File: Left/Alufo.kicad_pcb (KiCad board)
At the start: 2 copper layers, 139.7 x 88.9 mm, 67 parts, among them J1 USB_C_Receptacle_USB2.0_16P_2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, J3 USB_C_Receptacle_USB2.0_16P_2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, K11 PG1350, K12 PG1350, K13 PG1350, K14 PG1350, K15 PG1350, K16 PG1350, K21 PG1350, K22 PG1350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

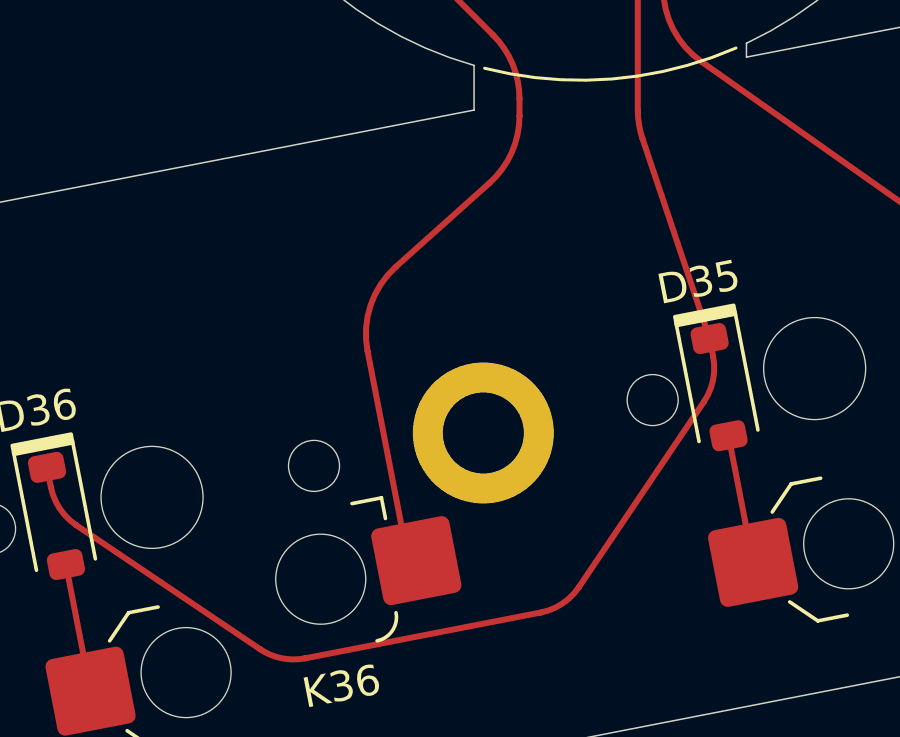
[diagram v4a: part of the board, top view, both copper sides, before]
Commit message: Fix alignment of thumb cluster screw hole
It did not line up when one side’s PCB was used as a base for the other.
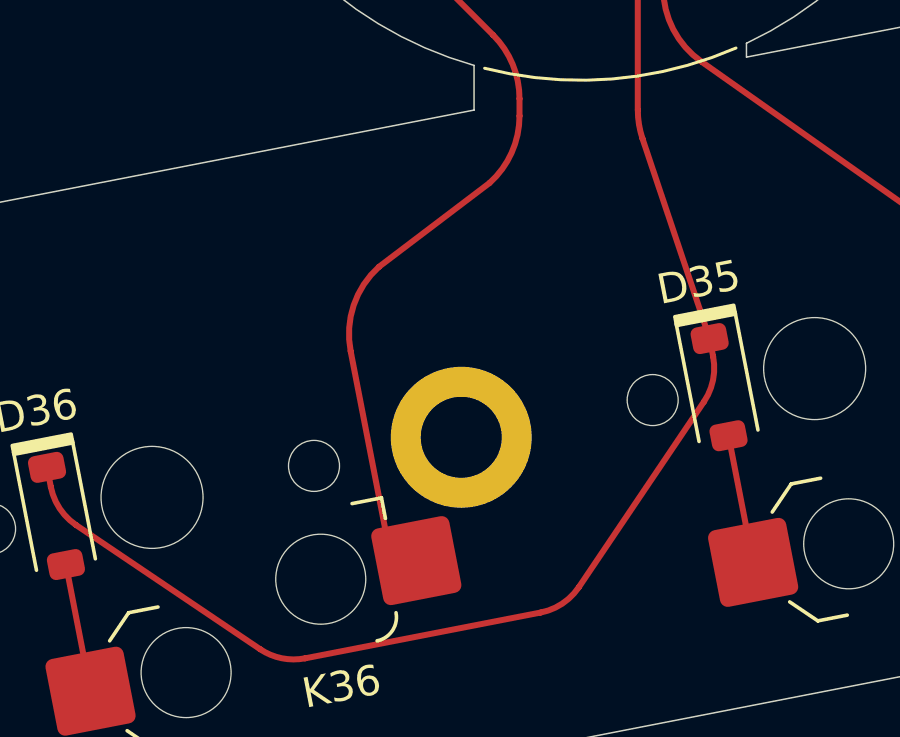
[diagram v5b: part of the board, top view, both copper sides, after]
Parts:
- moved H5 0.75 mm to (119.8, 102.8)
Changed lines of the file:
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@@
 	(footprint "Project Library:MountingHole_2.2mm_M2_SMD_Solder_Nut"
 		(layer "F.Cu")
-		(at 120.581105 102.686759)
+		(at 119.844885 102.829865)
 		(descr "Mounting Hole 2.2mm, M2, DIN965")
 		(tags "mounting hole 2.2mm m2 din965")
@@
 		(fp_arc
 			(start 1.749484 0.919719)
-			(mid 1.712517 0.81407)
+			(mid 1.712511 0.81407)
 			(end 1.699999 0.702842)
 			(stroke
@@
 		(fp_arc
 			(start 1.699999 -0.702843)
-			(mid 1.712527 -0.814069)
+			(mid 1.712528 -0.814069)
 			(end 1.749484 -0.919721)
 			(stroke
@@
 		(fp_arc
 			(start -1.749484 -0.919721)
-			(mid -1.638071 -1.504036)
+			(mid -1.638071 -1.504035)
 			(end -1.046711 -1.568299)
 			(stroke
@@
 	)
 	(gr_line
+		(start 109.5378 104.833359)
+		(end 119.844885 102.829865)
+		(stroke
+			(width 0.2)
+			(type default)
+		)
+		(layer "Cmts.User")
+	)
+	(gr_line
 		(start 150.8125 148.750035)
 		(end 153.9875 148.750035)
@@
 	)
 	(segment
-		(start 116.721052 99.956281)
-		(end 118.038342 106.733149)
+		(start 116.15771 99.956281)
+		(end 117.475 106.733149)
 		(width 0.2)
 		(layer "F.Cu")
@@
 	)
 	(segment
-		(start 113.898679 82.412679)
-		(end 120.908205 89.422205)
+		(start 117.101864 97.148436)
+		(end 120.787611 94.353845)
 		(width 0.2)
 		(layer "F.Cu")
@@
 	)
 	(segment
-		(start 120.787611 94.353845)
-		(end 117.665206 97.148436)
+		(start 113.898679 82.412679)
+		(end 120.908205 89.422205)
 		(width 0.2)
 		(layer "F.Cu")
@@
 	)
 	(arc
-		(start 117.665206 97.148436)
-		(mid 116.822387 98.427694)
-		(end 116.721052 99.956281)
+		(start 117.101864 97.148436)
+		(mid 116.259045 98.427694)
+		(end 116.15771 99.956281)
 		(width 0.2)
 		(layer "F.Cu")

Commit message: Add lefthand plate
The plate file is arranged to the left of the main PCB. This arrangement is a little more costly  than if the plate were upside down under the PCB. However, the cost difference is small (~$3 for a five-PCB run) and this way makes it easier to crosscheck and make matching adjustments to the plate and the PCB.
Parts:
- added H10: ScrewHole, MountingHole:MountingHole_2.2mm_M2, F.Cu at (62.7, 102.8)
- added H6: ScrewHole, MountingHole:MountingHole_2.2mm_M2, F.Cu at (56.9, 60.5)
- added H7: ScrewHole, MountingHole:MountingHole_2.2mm_M2, F.Cu at (95.2, 48.2)
- added H8: ScrewHole, MountingHole:MountingHole_2.2mm_M2, F.Cu at (95.2, 70.8)
- added H9: ScrewHole, MountingHole:MountingHole_2.2mm_M2, F.Cu at (133.6, 60.5)
- added PK11: SwitchHole, Project Library:SW_choc_v1_Plate_CPG135001S30_1u, F.Cu at (142.9, 52.4)
- added PK12: SwitchHole, Project Library:SW_choc_v1_Plate_CPG135001S30_1u, F.Cu at (123.8, 43.9)
- added PK13: SwitchHole, Project Library:SW_choc_v1_Plate_CPG135001S30_1u, F.Cu at (104.8, 39.7)
- added PK14: SwitchHole, Project Library:SW_choc_v1_Plate_CPG135001S30_1u, F.Cu at (85.7, 39.7)
- added PK15: SwitchHole, Project Library:SW_choc_v1_Plate_CPG135001S30_1u, F.Cu at (66.7, 43.9)
- added PK16: SwitchHole, Project Library:SW_choc_v1_Plate_CPG135001S30_1u, F.Cu at (47.6, 52.4)
- added PK21: SwitchHole, Project Library:SW_choc_v1_Plate_CPG135001S30_1u, F.Cu at (142.9, 69.4)
- added PK22: SwitchHole, Project Library:SW_choc_v1_Plate_CPG135001S30_1u, F.Cu at (123.8, 60.9)
- added PK23: SwitchHole, Project Library:SW_choc_v1_Plate_CPG135001S30_1u, F.Cu at (104.8, 56.7)
- added PK24: SwitchHole, Project Library:SW_choc_v1_Plate_CPG135001S30_1u, F.Cu at (85.7, 56.7)
- added PK25: SwitchHole, Project Library:SW_choc_v1_Plate_CPG135001S30_1u, F.Cu at (66.7, 60.9)
- added PK26: SwitchHole, Project Library:SW_choc_v1_Plate_CPG135001S30_1u, F.Cu at (47.6, 69.4)
- added PK31: SwitchHole, Project Library:SW_choc_v1_Plate_CPG135001S30_1u, F.Cu at (123.8, 77.9)
- added PK32: SwitchHole, Project Library:SW_choc_v1_Plate_CPG135001S30_1u, F.Cu at (104.8, 73.7)
- added PK33: SwitchHole, Project Library:SW_choc_v1_Plate_CPG135001S30_1u, F.Cu at (85.7, 73.7)
- added PK34: SwitchHole, Project Library:SW_choc_v1_Plate_CPG135001S30_1u, F.Cu at (66.7, 77.9)
- added PK35: SwitchHole, Project Library:SW_choc_v1_Plate_CPG135001S30_1u, F.Cu at (74.5, 100.5)
- added PK36: SwitchHole, Project Library:SW_choc_v1_Plate_CPG135001S30_1.5u, F.Cu at (52.4, 104.8)
- H1, H2, H3, H4, H5: value MountingHole -> SolderNut
- moved L1 85.7 mm to (238.1, 33.6)
- moved R13 85.7 mm to (255.9, 54.3)
- moved C1 85.7 mm to (181.5, 58.4)
- moved C3 85.7 mm to (181.5, 60.0)
- moved C5 85.7 mm to (187.4, 51.3)
- moved D15 85.7 mm to (206.3, 44.1)
- moved D34 85.7 mm to (206.3, 76.3)
- moved FB1 85.7 mm to (182.6, 47.8)
- moved K15 85.7 mm to (209.6, 43.9)
- moved K25 85.7 mm to (209.6, 60.9)
- moved K34 85.7 mm to (209.6, 77.9)
- moved NT1 85.7 mm to (180.0, 63.2)
- moved R1 85.7 mm to (177.7, 53.6)
- moved R16 85.7 mm to (198.7, 66.8)
- moved U3 85.7 mm to (175.5, 53.6)
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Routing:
- added copper zone on F.Cu, net (none)
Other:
- board size 139.7 x 88.9 mm -> 282.6 x 88.9 mm

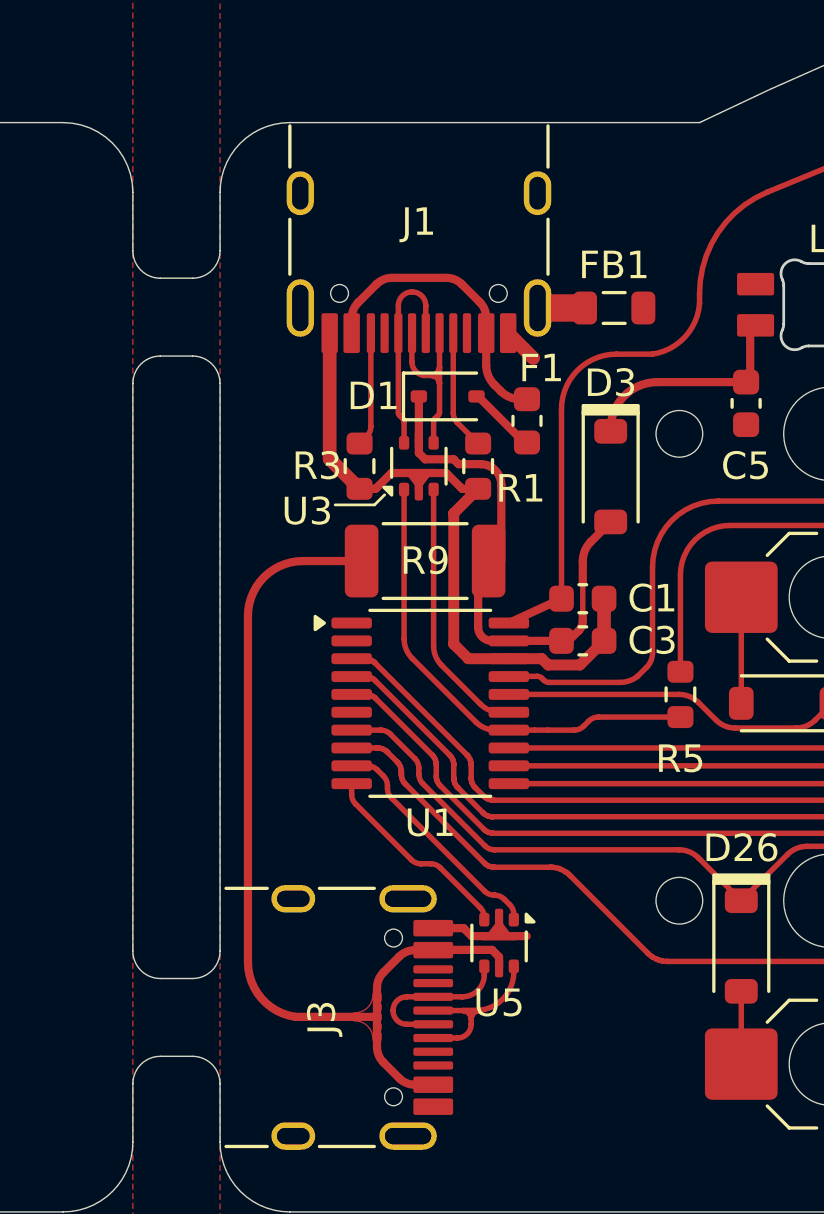
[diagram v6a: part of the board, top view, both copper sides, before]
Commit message: Add order number location
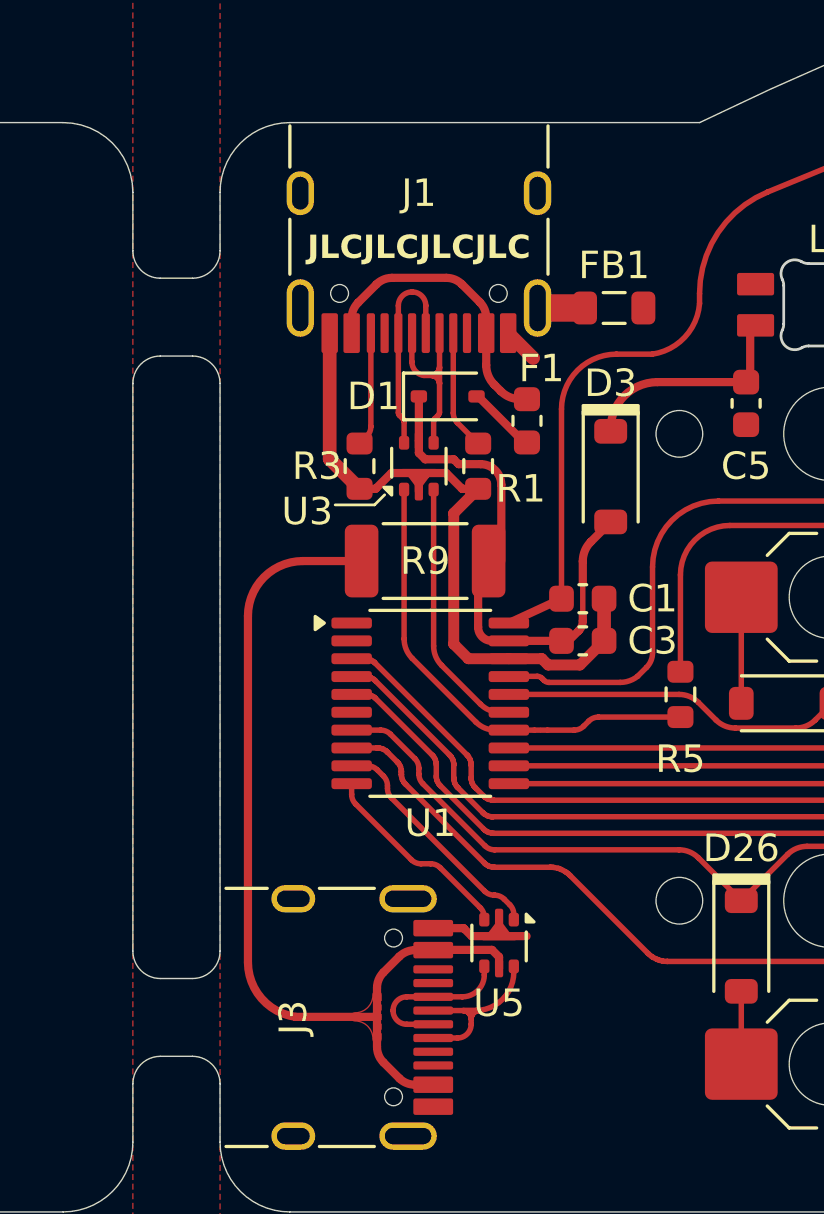
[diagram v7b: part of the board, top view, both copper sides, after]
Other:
- board text added: "JLCJLCJLCJLC"
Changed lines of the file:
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@@
 		(tags "usb usb-c 2.0 pd")
 		(property "Reference" "J1"
-			(at 0 0 0)
+			(at 0 1.05 0)
 			(layer "F.SilkS")
 			(effects
@@
 		)
 		(fp_text user "${REFERENCE}"
-			(at 0 0 0)
+			(at 0 1.05 0)
 			(layer "F.Fab")
 			(effects
@@
 		(tags "usb usb-c 2.0 pd")
 		(property "Reference" "J3"
-			(at 0 0 90)
+			(at 0 1.05 90)
 			(layer "F.SilkS")
 			(effects
@@
 		)
 		(fp_text user "${REFERENCE}"
-			(at 0 0 90)
+			(at 0 1.05 90)
 			(layer "F.Fab")
 			(effects
@@
 		(layer "User.4")
 	)
+	(gr_text "JLCJLCJLCJLC"
+		(at 175.517 45.619 0)
+		(layer "F.SilkS")
+		(effects
+			(font
+				(size 0.85 0.85)
+				(thickness 0.16)
+				(bold yes)
+			)
+		)
+	)
 	(gr_text "${TITLE} v${REVISION} • ${COMPANY}"

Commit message: Update plate outline
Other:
- outline, holes or cut-outs redrawn
- board text removed: "LED"
